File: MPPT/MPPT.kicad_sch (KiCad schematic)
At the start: 18 parts, among them T1 Q_NMOS_GDS, T2 Q_NMOS_GDS, T3 Transformer_1P_1S, U1 5962R1822201VXC, U2 SN0048HBX

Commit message: Se cambia el esquemático para usar la plantilla
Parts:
- removed D3: D, symbol Device:D
- removed T1, T2: Q_NMOS_GDS, symbol Transistor_FET:Q_NMOS_GDS
- removed T3: Transformer_1P_1S, symbol Device:Transformer_1P_1S
- removed U2: SN0048HBX, HBX0048A-C01-MFG, symbol 595-SN0048HBX:SN0048HBX
- added C10, C11, C5, C6, C7, C8, C9: C_US, symbol Device:C_US
- added C12, C8: C, symbol Device:C
- added C3: 0.1uF, Capacitor_SMD:C_0805_2012Metric, symbol Device:C
- added D1, D2: D, symbol Device:D
- added H1, H2: Stack Header, Connector_PinHeader_2.54mm:PinHeader_2x26_P2.54mm_Vertical, symbol Connector_Generic:Conn_02x26_Odd_Even
- added L1, L2: L, symbol Device:L
- added MH1, MH2, MH3, MH4: M3, MountingHole:MountingHole_3.2mm_M3_Pad, symbol Mechanical:MountingHole_Pad
- added Q1, Q2, Q3, Q4: BS108, Package_TO_SOT_THT:TO-92_Inline, symbol Transistor_FET:BS108
- added R10, R11, R12, R13, R14, R15, R2, R8, R9: R, symbol Device:R
- added TR1: Wuerth_750315371, Transformer_SMD:Transformer_Wuerth_750315371, symbol Transformer:Wuerth_750315371
- added U2, U3, U4, U5: UCC27511DBVR, DBV0006A_N, symbol UCC27511:UCC27511DBVR
- added U6: ISOS141FDBQSEP, SSOP16_DBQ_TEX, symbol ISOS141FDBQSEP:ISOS141FDBQSEP
- C1, C2, C4: value C -> 0.1uF; footprint (none) -> Capacitor_SMD:C_0805_2012Metric
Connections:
- net COMP: now also C5.1, C6.1; no longer C1.1, C2.1
- net GND: now also C2.2, C3.2, H2.21 (Pin_21), H2.22 (Pin_22), H2.29 (Pin_29), H2.30 (Pin_30), H2.31 (Pin_31), H2.32 (Pin_32); no longer C5.2, R1.2, R5.2, R6.2, U1.14 (AVSS)
- net OUTA: now also U3.6 (IN+)
- net OUTB: now also U2.6 (IN+)
- net at R5.1: now also R4.2, Q4.2 (G)
- net at R1.1: now also C5.2; no longer C2.2
- net at R3.2: now also Q3.2 (G), R2.1
- net at C7.2: now also R6.2, D1.1 (K), D2.1 (K); no longer C6.2
- net SRB: now reaches U1.12 (SRB)
- net SRB: now also U6.4 (INB)
- net SRA: now reaches U1.13 (SRA)
- net SRA: now also U6.3 (INA)
- net CS_ILIM: now reaches U1.16 (CS_ILIM)
- net CS_ILIM: now also C12.1, R15.1
- net at R7.2: now also U4.2 (OUTH); no longer C7.1
- net at R3.1: now also U2.3 (OUTL)
- net at C4.1: now also MH4.1
- net at R6.1: now also C7.1
- net at R4.1: now also U3.2 (OUTH)
- net at R7.1: now also Q1.2 (G), R8.2
- new net: C2.1, MH2.1
- new net: C1.1, MH1.1
- new net: C3.1, MH3.1
- new net: C8.1, L1.2, L2.1, R11.1
- new net: C10.1, C11.1, C5.1, C6.1, C7.1, C8.1, C9.1, L2.2, R11.2, R12.1
- new net: R2.2, U2.2 (OUTH)
- new net: Q2.1 (D), TR1.6
- new net: Q2.2 (G), R10.1, R9.2
- new net: L1.1, TR1.5
- new net: R5.2, U3.3 (OUTL)
- new net: R12.2, R13.1
- new net: R9.1, U5.2 (OUTH)
- new net: R10.2, U5.3 (OUTL)
- new net: U5.6 (IN+), U6.13 (OUTB)
- new net: R8.1, U4.3 (OUTL)
- new net: D2.2 (A), Q3.1 (D), TR1.1
- new net: U4.6 (IN+), U6.14 (OUTA)
- new net: Q1.1 (D), TR1.4
- new net +3V3: H2.27 (Pin_27), H2.28 (Pin_28)
- new net +5V: H2.25 (Pin_25), H2.26 (Pin_26)
- new net +BATT: H2.45 (Pin_45), H2.46 (Pin_46)
- new net 5VIN: H1.32 (Pin_32)
- new net A: D1.2 (A), Q4.1 (D), TR1.3
- new net BCR_OUT: H2.41 (Pin_41), H2.42 (Pin_42), H2.43 (Pin_43), H2.44 (Pin_44)
- new net CRX3/GP30: H1.29 (Pin_29)
- new net CS: Q3.3 (S), Q4.3 (S), R14.1, R15.2
- new net CS/GP10: H1.46 (Pin_46)
- new net CS/GP36: H1.50 (Pin_50)
- new net CS/GP37: H1.48 (Pin_48)
- new net CTX3/GP31: H1.31 (Pin_31)
- new net GND1: C12.2, C6.2, R1.2, R14.2, U1.14 (AVSS), U2.4 (GND), U2.5 (IN-), U3.4 (GND), U3.5 (IN-), U6.2 (GND1), U6.8 (GND1)
- new net GND2: C10.2, C11.2, C5.2, C6.2, C7.2, C8.2, C8.2, C9.2, Q1.3 (S), Q2.3 (S), R13.2, U4.4 (GND), U4.5 (IN-), U5.4 (GND), U5.5 (IN-), U6.15 (GND2), U6.9 (GND2)
- new net GP14/A0/TX3: H1.15 (Pin_15)
- new net GP15/A1/RX3: H1.13 (Pin_13)
- new net GP2: H1.4 (Pin_4)
- new net GP20/A6/TX5: H1.19 (Pin_19)
- new net GP21/A7/RX5: H1.17 (Pin_17)
- new net GP22/A8: H1.18 (Pin_18)
- new net GP23/A9: H1.16 (Pin_16)
- new net GP3: H1.6 (Pin_6)
- new net GP32: H1.28 (Pin_28)
- new net GP33: H1.30 (Pin_30)
- new net GP38/A14: H1.26 (Pin_26)
- new net GP39/A15: H1.24 (Pin_24)
- new net GP4: H1.8 (Pin_8)
- new net GP40/A16: H1.22 (Pin_22)
- new net GP41/A17: H1.20 (Pin_20)
- new net GP5: H1.10 (Pin_10)
- new net GP6: H1.12 (Pin_12)
- new net GP9: H1.14 (Pin_14)
- new net MISO0: H1.38 (Pin_38)
- new net MISO1: H1.44 (Pin_44)
- new net MOSI0: H1.36 (Pin_36)
- new net MOSI1: H1.42 (Pin_42)
- new net PCM_IN: H2.35 (Pin_35), H2.36 (Pin_36)
- new net RX1/GP0: H1.5 (Pin_5)
- new net RX2/GP7: H1.9 (Pin_9)
- new net RX7/GP28: H1.21 (Pin_21)
- new net RX8/GP34: H1.25 (Pin_25)
- new net SCK0: H1.34 (Pin_34)
- new net SCK1: H1.40 (Pin_40)
- new net SCL0: H1.43 (Pin_43)
- new net SCL1: H1.39 (Pin_39)
- new net SCL2: H1.35 (Pin_35)
- new net SDA0: H1.41 (Pin_41)
- new net SDA1: H1.37 (Pin_37)
- new net SDA2: H1.33 (Pin_33)
- new net SW1: H2.9 (Pin_9)
- new net SW10: H2.18 (Pin_18)
- new net SW11: H2.19 (Pin_19)
- new net SW12: H2.20 (Pin_20)
- new net SW2: H2.10 (Pin_10)
- new net SW3: H2.11 (Pin_11)
- new net SW4: H2.12 (Pin_12)
- new net SW5: H2.13 (Pin_13)
- new net SW6: H2.14 (Pin_14)
- new net SW7: H2.15 (Pin_15)
- new net SW8: H2.16 (Pin_16)
- new net SW9: H2.17 (Pin_17)
- new net TX1/GP1: H1.7 (Pin_7)
- new net TX2/GP8: H1.11 (Pin_11)
- new net TX7/GP29: H1.23 (Pin_23)
- new net TX8/GP35: H1.27 (Pin_27)
- no-connect marks 0 -> 8
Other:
- moved on the sheet: R1, U1

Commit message: Se reestructura el esquemático para tener una visión más clara
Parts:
- removed C10, C11, C5, C6, C7, C8, C9: C_US, symbol Device:C_US
- added C10, C11, C13, C14, C15, C16, C9: C_Polarized, symbol Device:C_Polarized
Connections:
- net GND2: now also C10.2, C11.2, C13.2, C14.2, C15.2, C16.2, C9.2
- net at L2.2, R11.2, R12.1: now also C10.1, C11.1, C13.1, C14.1, C15.1, C16.1, C9.1
- net OUT_DC: now reaches L1.1, TR1.5
- net SRB2: now reaches U5.6 (IN+), U6.13 (OUTB)
- net SRA2: now reaches U4.6 (IN+), U6.14 (OUTA)
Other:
- note added: "Aislador digital"
- note added: "Compensador"
- note added: "Controlador"
- note added: "Etapa DC-DC"
- note added: "Limitador"
- note added: "Salida"
- moved on the sheet: C1, C12, C2, C3, C4, C5, C6, C7, C8, D1, D2, H1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

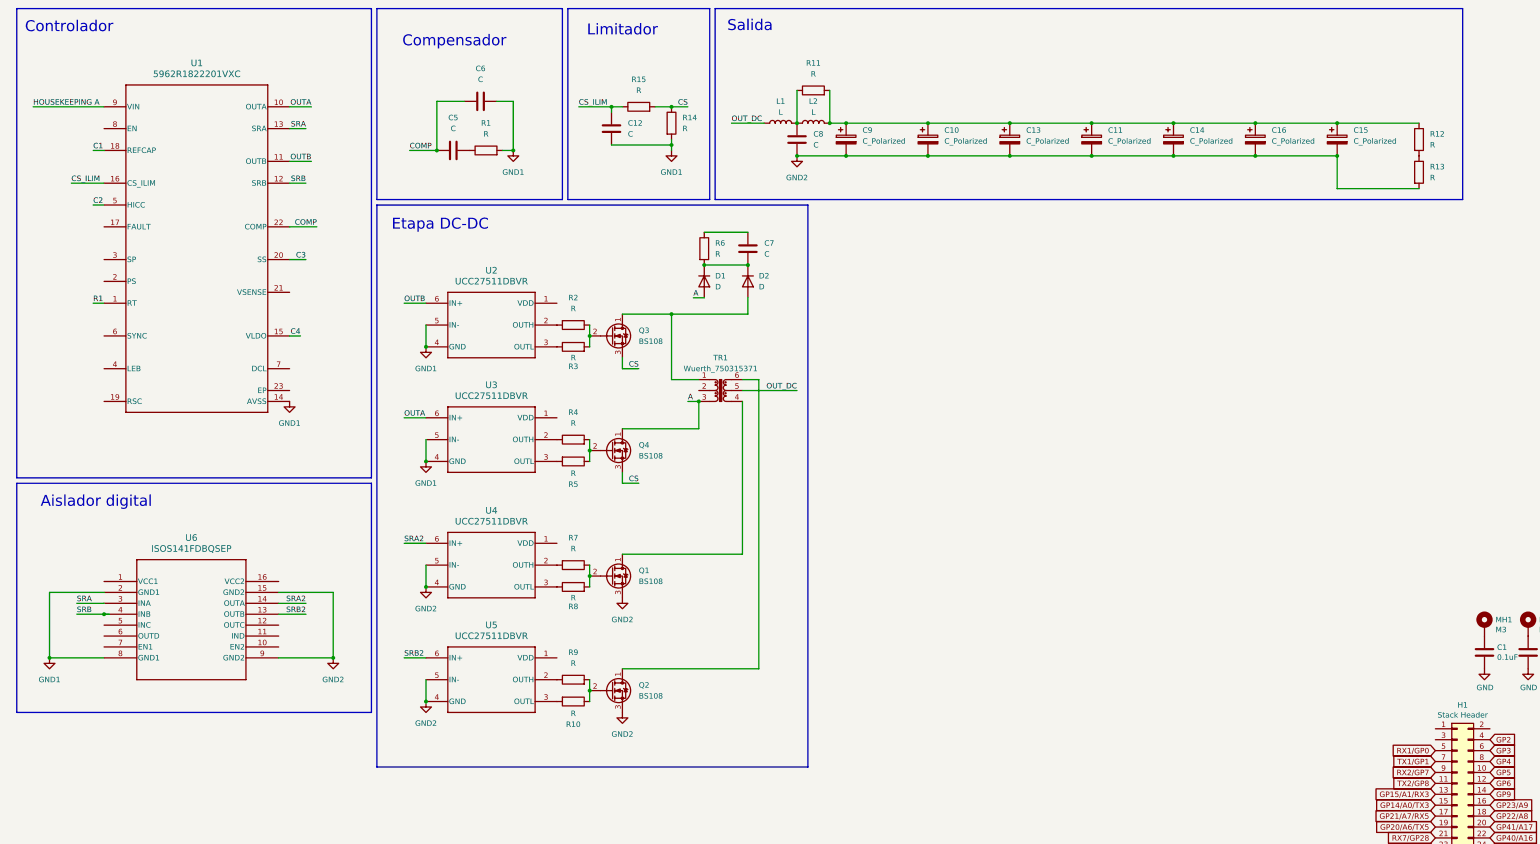
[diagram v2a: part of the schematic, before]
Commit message: Se empieza con el diseño buck
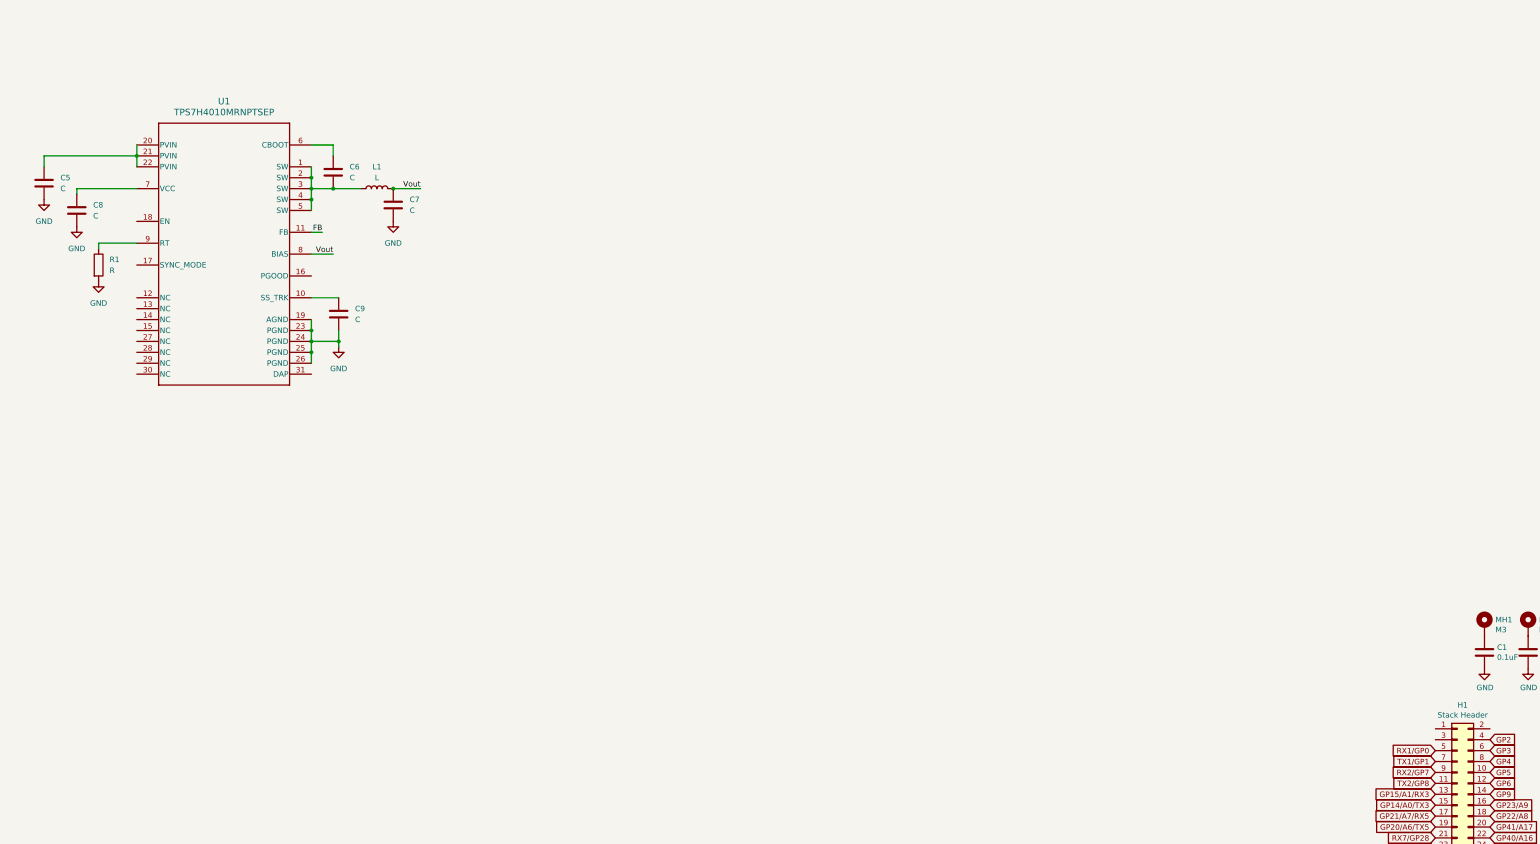
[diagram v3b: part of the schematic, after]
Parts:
- removed C10, C11, C13, C14, C15, C16, C9: C_Polarized, symbol Device:C_Polarized
- removed C12: C, symbol Device:C
- removed D1, D2: D, symbol Device:D
- removed L2: L, symbol Device:L
- removed Q1, Q2, Q3, Q4: BS108, Package_TO_SOT_THT:TO-92_Inline, symbol Transistor_FET:BS108
- removed R10, R11, R12, R13, R14, R15, R2, R3, R4, R5, R6, R7, R8, R9: R, symbol Device:R
- removed TR1: Wuerth_750315371, Transformer_SMD:Transformer_Wuerth_750315371, symbol Transformer:Wuerth_750315371
- removed U1: 5962R1822201VXC, HFT0022A-C01-MFG, symbol 5962R1822201VXC:5962R1822201VXC
- removed U2, U3, U4, U5: UCC27511DBVR, DBV0006A_N, symbol UCC27511:UCC27511DBVR
- removed U6: ISOS141FDBQSEP, SSOP16_DBQ_TEX, symbol ISOS141FDBQSEP:ISOS141FDBQSEP
- added C9: C, symbol Device:C
- added U1: TPS7H4010MRNPTSEP, RNP0030A-MFG, symbol TPS7H4010MRNPTSEP:TPS7H4010MRNPTSEP
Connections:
- net GND2 is gone; now on net GND: C8.2
- net OUT_DC is gone; now on an unnamed net: L1.1
- net GND: now also C5.2, C7.2, R1.2, C9.2, U1.19 (AGND), U1.23 (PGND), U1.24 (PGND), U1.25 (PGND), U1.26 (PGND)
- net at C8.1: now also U1.7 (VCC); no longer L1.2
- net at R1.1: now also U1.9 (RT); no longer C5.2
- net Vout: now reaches C7.1
- net Vout: now also L1.2, U1.8 (BIAS)
- net COMP: no longer names the net of C5.1
- net COMP: now also U1.20 (PVIN), U1.21 (PVIN), U1.22 (PVIN); no longer C6.1
- net GND1: no longer names the net of C6.2
- net GND1: now also U1.1 (SW), U1.2 (SW), U1.3 (SW), U1.4 (SW), U1.5 (SW); no longer R1.2
- new net: C9.1, U1.10 (SS_TRK)
- new net: C6.1, U1.6 (CBOOT)
- new net FB: U1.11 (FB)
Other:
- note removed: "Aislador digital"
- note removed: "Compensador"
- note removed: "Controlador"
- note removed: "Etapa DC-DC"
- note removed: "Limitador"
- note removed: "Salida"

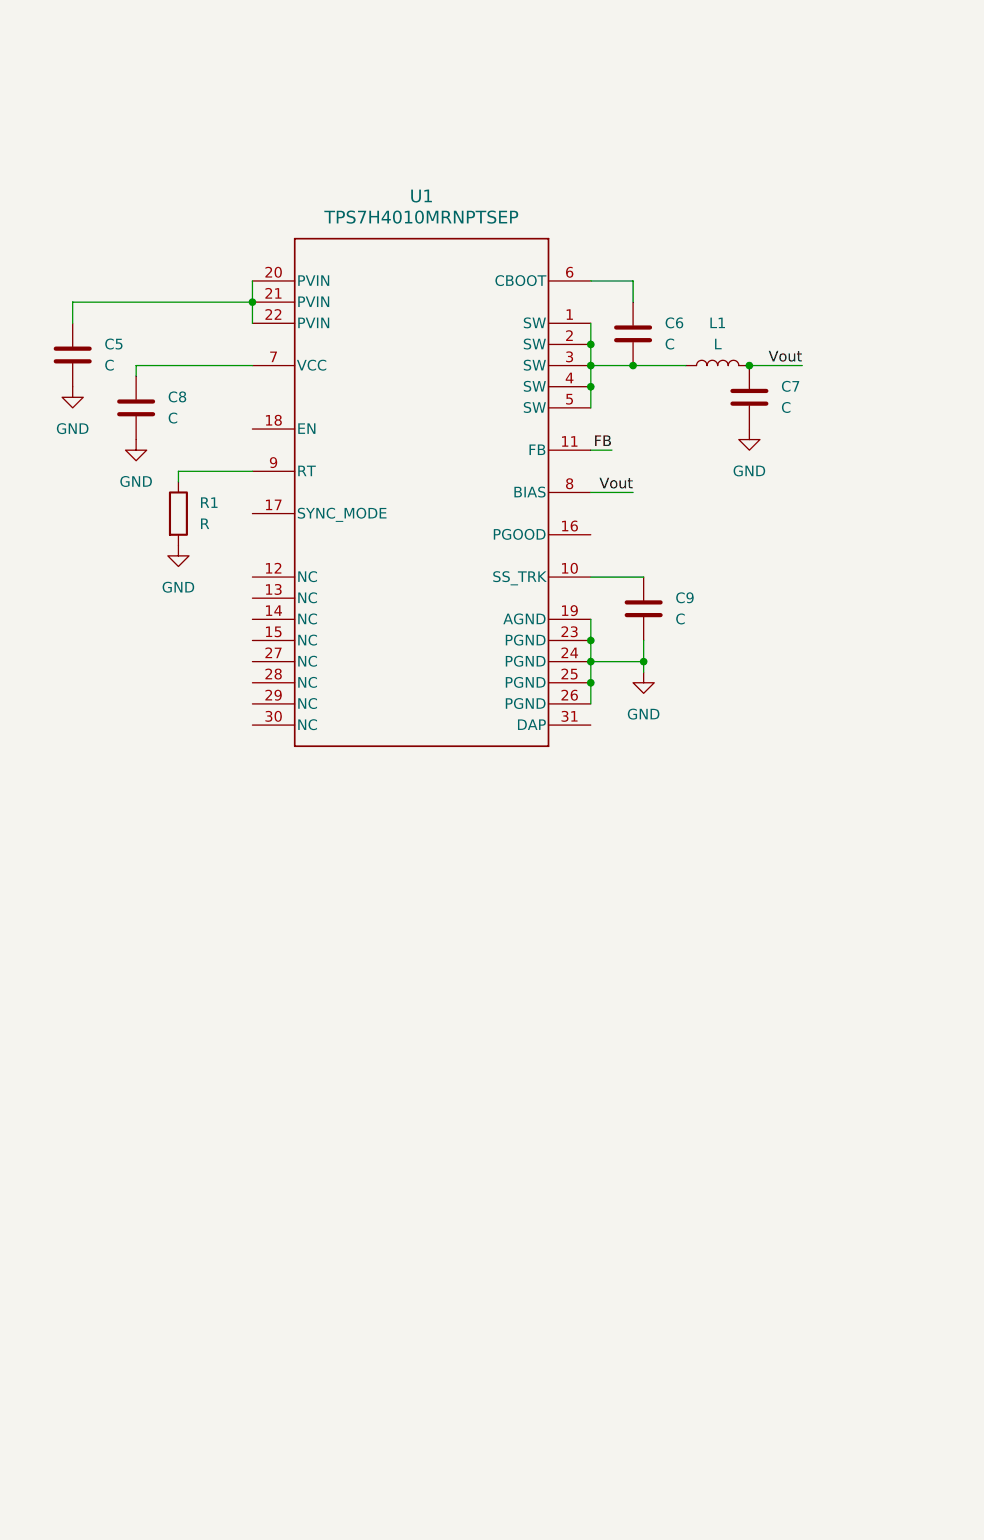
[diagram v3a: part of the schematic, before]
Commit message: Se hizo el censado del voltaje y corriente del panel
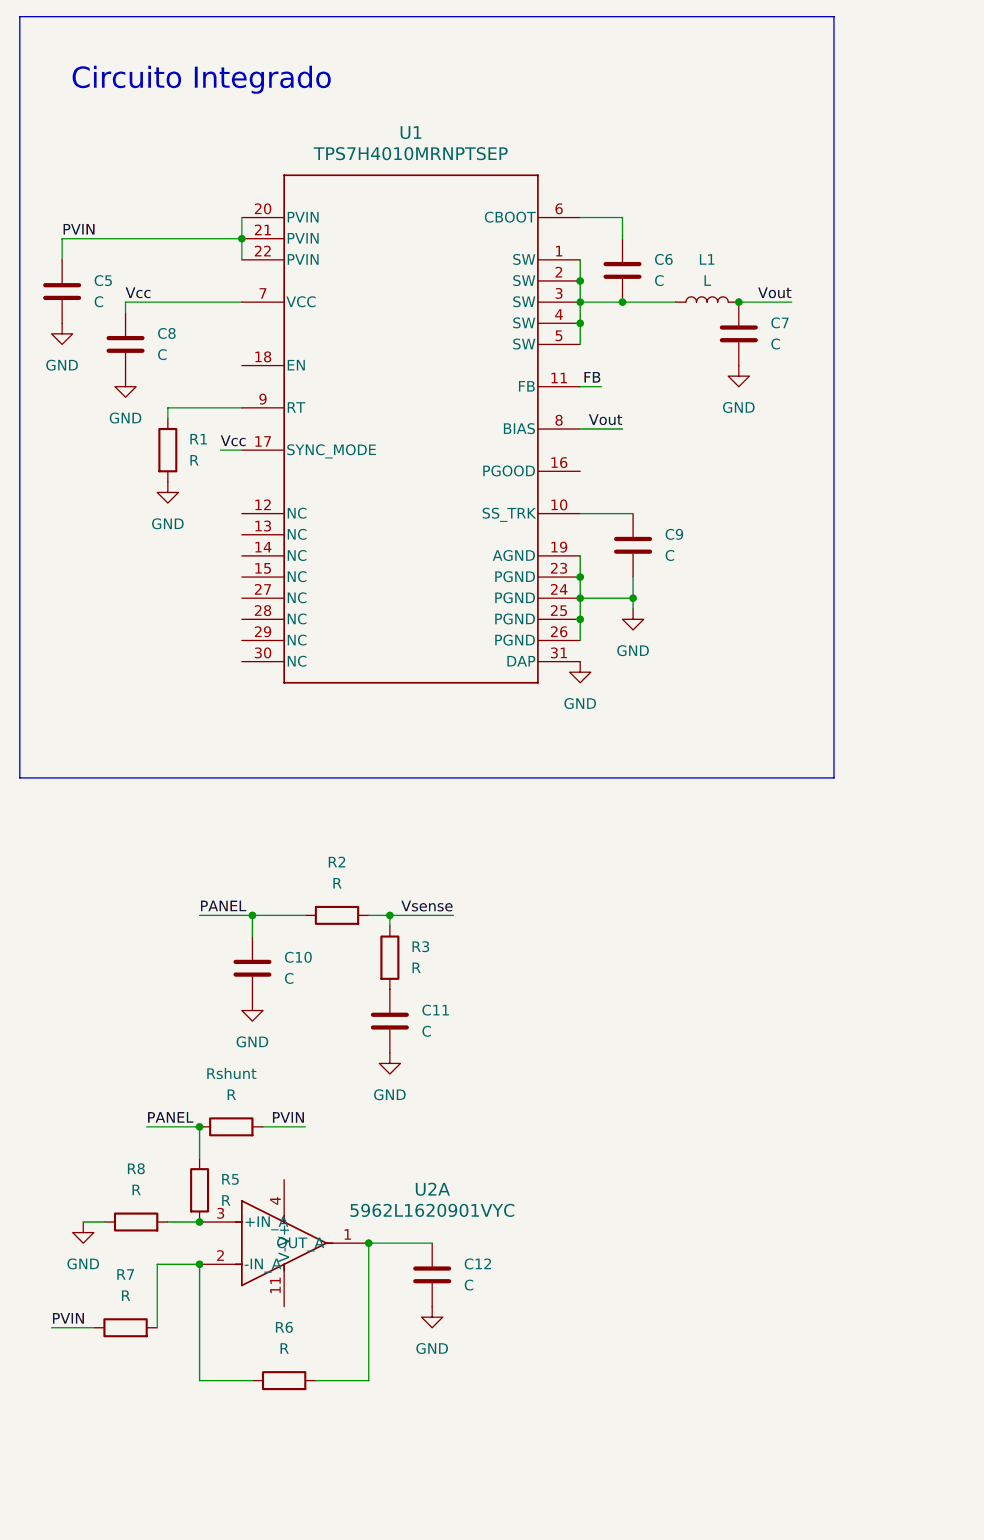
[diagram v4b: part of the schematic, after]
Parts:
- added C10, C11, C12: C, symbol Device:C
- added R2, R3, R5, R6, R7, R8, Rshunt: R, symbol Device:R
- added U2: 5962L1620901VYC, HFR0014A-IPC_A, symbol 5962L1620901VYC:5962L1620901VYC
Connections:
- net GND: now also U1.31 (DAP), C10.2, C11.2, C12.2, R8.1
- net Vcc: now reaches U1.17 (SYNC_MODE)
- net Vcc: now also C8.1, U1.7 (VCC)
- net PVIN: now reaches C5.1, U1.20 (PVIN), U1.21 (PVIN), U1.22 (PVIN)
- net PVIN: now also R7.1, Rshunt.2
- new net: C11.1, R3.2
- new net: R5.2, R8.2, U2.3 (+IN_A)
- new net: R6.1, R7.2, U2.2 (-IN_A)
- new net: C12.1, R6.2, U2.1 (OUT_A)
- new net PANEL: C10.1, R2.1, R5.1, Rshunt.1
- new net Vsense: R2.2, R3.1
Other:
- note added: "Circuito Integrado"
- moved on the sheet: C5, C6, C7, C8, C9, L1, R1, U1
